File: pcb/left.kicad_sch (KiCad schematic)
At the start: 65 parts, among them SW1 SW_PUSH, SW10 SW_PUSH, SW11 SW_PUSH, SW12 SW_PUSH, SW13 SW_PUSH, SW14 SW_PUSH, SW15 SW_PUSH, SW16 SW_PUSH, SW17 SW_PUSH, SW18 SW_PUSH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

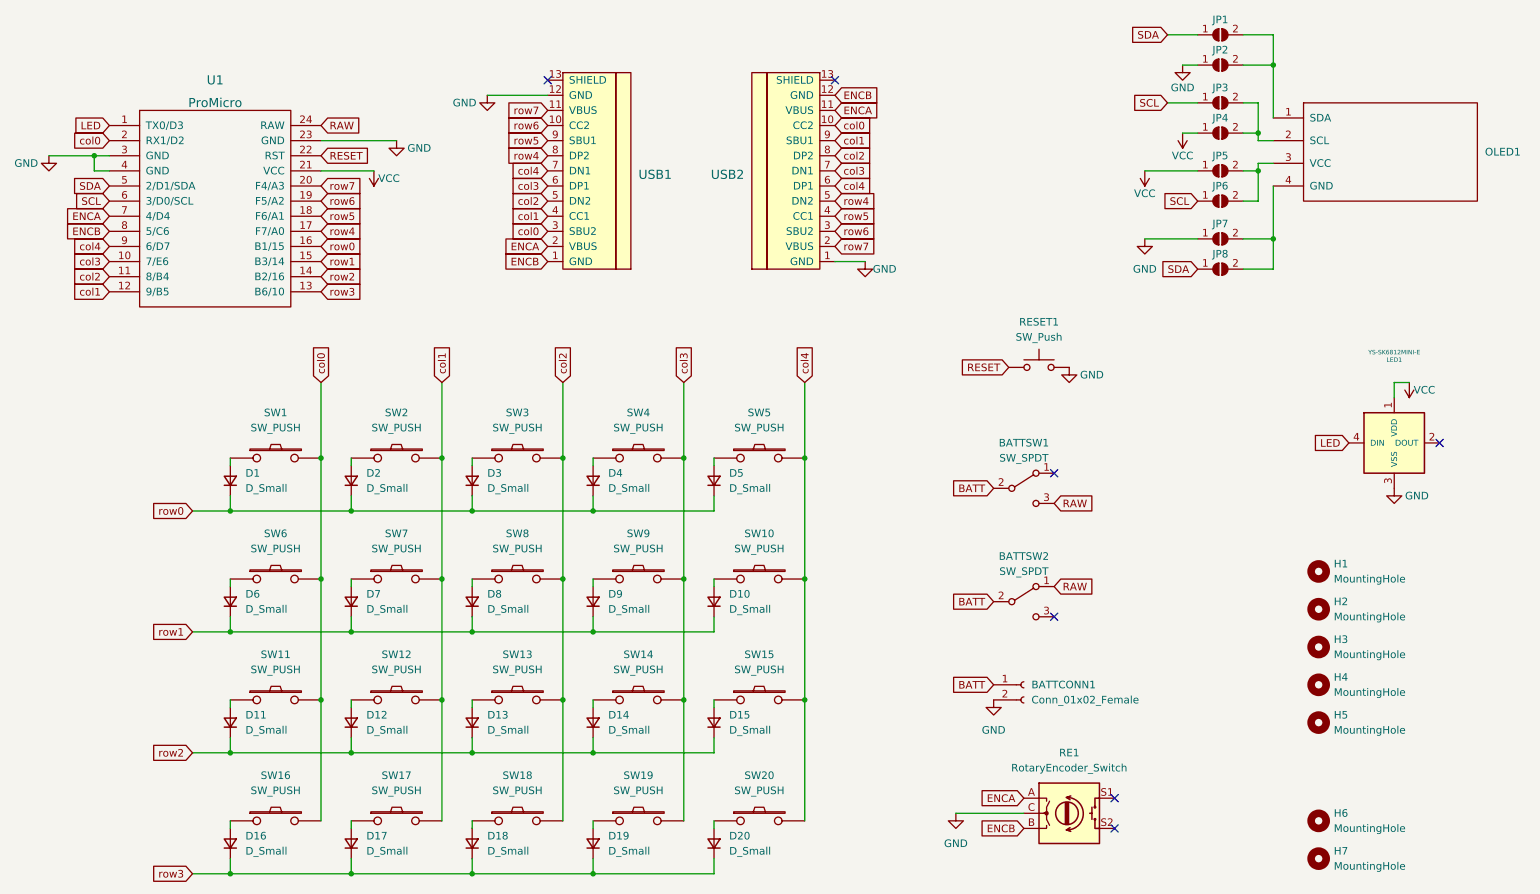
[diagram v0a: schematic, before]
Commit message: separate left and right sides
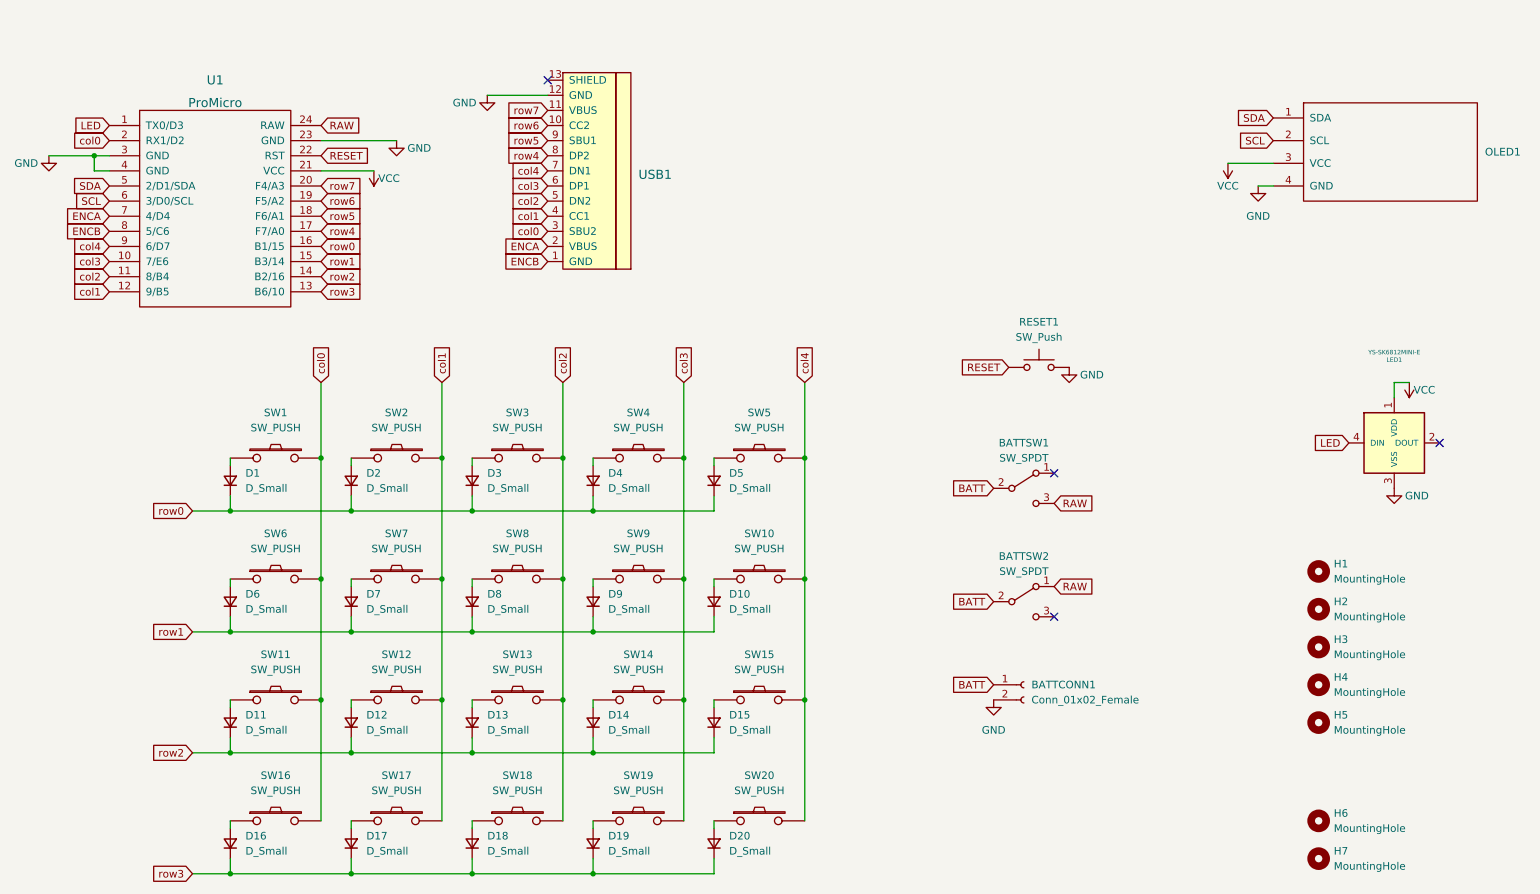
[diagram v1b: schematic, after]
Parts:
- removed JP1, JP2, JP3, JP4, JP5, JP6, JP7, JP8: SolderJumper_2_Open, Jumper:SolderJumper-2_P1.3mm_Open_TrianglePad1.0x1.5mm, symbol Jumper:SolderJumper_2_Open
- removed RE1: RotaryEncoder_Switch, pica:RotaryEncoder_EC11-no-legs, symbol Device:RotaryEncoder_Switch
- removed USB2: HRO-TYPE-C-31-M-12, typec:HRO-TYPE-C-31-M-12-HandSoldering, symbol typec:HRO-TYPE-C-31-M-12
- RESET1: footprint kbd:ResetSW -> kbd:ResetSW_1side
- U1: footprint keebio:ArduinoProMicro -> pica:ProMicro
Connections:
- net GND: now also OLED1.4 (GND)
- net SCL: now also OLED1.2 (SCL)
- net SDA: now also OLED1.1 (SDA)
- net VCC: now also OLED1.3 (VCC)
- no-connect marks 7 -> 4

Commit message: fix battery connector footprint
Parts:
- BATTCONN1: footprint Connector_JST:JST_XH_S2B-XH-A_1x02_P2.50mm_Horizontal -> Connector_JST:JST_PH_S2B-PH-K_1x02_P2.00mm_Horizontal
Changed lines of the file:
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@@
       (effects (font (size 1.27 1.27)) (justify left))
     )
-    (property "Footprint" "Connector_JST:JST_XH_S2B-XH-A_1x02_P2.50mm_Horizontal" (id 2) (at 187.96 129.54 0)
+    (property "Footprint" "Connector_JST:JST_PH_S2B-PH-K_1x02_P2.00mm_Horizontal" (id 2) (at 187.96 129.54 0)
       (effects (font (size 1.27 1.27)) hide)
     )
@@
     )
     (path "/39669874-ccc4-4e68-8529-233aa9d084b4"
-      (reference "BATTCONN1") (unit 1) (value "Conn_01x02_Female") (footprint "Connector_JST:JST_XH_S2B-XH-A_1x02_P2.50mm_Horizontal")
+      (reference "BATTCONN1") (unit 1) (value "Conn_01x02_Female") (footprint "Connector_JST:JST_PH_S2B-PH-K_1x02_P2.00mm_Horizontal")
     )
     (path "/b1f6a19b-fde1-4210-8161-211b835723ec"

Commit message: add full version
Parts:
- removed BATTSW2: SW_SPDT, Button_Switch_SMD:SW_SPDT_PCM12, symbol Switch:SW_SPDT
- removed LED1: YS-SK6812MINI-E, pica:SK6812-MINI-E, symbol kbd:YS-SK6812MINI-E
- removed OLED1: OLED, kbd:OLED_v2, symbol kbd:OLED
- removed RESET1: SW_Push, kbd:ResetSW_1side, symbol Switch:SW_Push
- removed U1: ProMicro, pica:ProMicro, symbol kbd:ProMicro
- added JP1, JP2: SolderJumper_2_Open, Jumper:SolderJumper-2_P1.3mm_Open_TrianglePad1.0x1.5mm, symbol Jumper:SolderJumper_2_Open
- added RE1: RotaryEncoder_Switch, pica:RotaryEncoder_EC11, symbol Device:RotaryEncoder_Switch
- added U1: xiao-ble, kleeb-mcu:xiao-ble-tht, symbol kleeb-mcu:xiao-ble
- USB1: footprint typec:HRO-TYPE-C-31-M-12-HandSoldering -> pica:HRO-TYPE-C-31-M-12-data
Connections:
- net row7 is gone; now on net VCC: USB1.11 (VBUS)
- net ENCA: now also RE1.A, U1.6 (A9_SCL/0.05_H); no longer USB1.2 (VBUS)
- net ENCB: now also USB1.5 (DN2), USB1.7 (DN1), JP1.1 (A), RE1.B; no longer USB1.1 (GND)
- net GND: now also USB1.1 (GND), RE1.C, U1.13 (GND), U1.18 (GND), U1.20 (GND)
- net RAW: now also U1.19 (BAT)
- net VCC: now also USB1.2 (VBUS), U1.12 (3V3)
- net col0: now also U1.1 (A2/0.02_H); no longer USB1.3 (SBU2)
- net col1: now also U1.2 (A4/0.03_H); no longer USB1.4 (CC1)
- net col2: now also U1.3 (A10/0.28); no longer USB1.5 (DN2)
- net col3: now also U1.4 (A11/0.29); no longer USB1.6 (DP1)
- net col4: now also U1.5 (A8_SDA/0.04_H); no longer USB1.7 (DN1)
- net row0: now also U1.11 (A6_MOSI/1.15)
- net row1: now also U1.10 (A5_MISO/1.14)
- net row2: now also U1.9 (A7_SCK/1.13)
- net row3: now also U1.8 (B9_RX/1.12)
- net row4 renamed DATA
- net DATA: now also USB1.6 (DP1), JP2.1 (A)
- net row5: no longer names the net of USB1.9 (SBU1)
- net row6: no longer names the net of USB1.10 (CC2)
- new net: JP1.2 (B), JP2.2 (B), U1.7 (B8_TX/1.11)
- no-connect marks 4 -> 14

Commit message: v2
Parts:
- added BATTCONN2: Conn_01x02_Female, pica:JST_PH_S2B-PH-K_1x02_P2.00mm, symbol Connector:Conn_01x02_Female
- added RE2: RotaryEncoder_Switch, pica:RotaryEncoder_EC11, symbol Device:RotaryEncoder_Switch
- BATTCONN1: footprint Connector_JST:JST_PH_S2B-PH-K_1x02_P2.00mm_Horizontal -> pica:JST_PH_S2B-PH-K_1x02_P2.00mm
- H1, H2, H3, H4, H5: footprint kbd:M2_HOLE_v2 -> pica:spacer_m2_3.4
- H6, H7: footprint kbd:M2_Hole_TH -> kbd:thread_m2
- SW1, SW10, SW11, SW12, SW13, SW14, SW15, SW16, SW17, SW18, SW19, SW2, SW3, SW4, SW5, SW6, SW7, SW8, SW9: footprint pica:CherryMX_Hotswap -> pica:CherryMX_Hotswap_ChocV2
- SW20: footprint pica:CherryMX_Hotswap_1.5 -> pica:CherryMX_Hotswap_ChocV2_1.5
- U1: footprint kleeb-mcu:xiao-ble-tht -> pica:xiao-ble-tht
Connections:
- net BATT: now also BATTCONN2.1 (Pin_1)
- net ENCA: now also RE2.A
- net ENCB: now also RE2.B
- net GND: now also BATTCONN2.2 (Pin_2), RE2.C
- no-connect marks 14 -> 16
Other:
- moved on the sheet: RE1

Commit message: remove second encoder
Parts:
- removed RE2: RotaryEncoder_Switch, pica:RotaryEncoder_EC11, symbol Device:RotaryEncoder_Switch
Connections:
- no-connect marks 16 -> 14
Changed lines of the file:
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@@
   (no_connect (at 106.68 29.21))
   (no_connect (at 163.83 55.88))
-  (no_connect (at 248.92 77.47))
   (no_connect (at 83.82 21.59))
-  (no_connect (at 248.92 82.55))
   (no_connect (at 248.92 57.15))
   (no_connect (at 163.83 30.48))
@@
     (stroke (width 0) (type default) (color 0 0 0 0))
   )
-  (wire (pts (xy 233.68 80.01) (xy 222.25 80.01))
-    (stroke (width 0) (type default) (color 0 0 0 0))
-  )
   (wire (pts (xy 135.89 118.11) (xy 135.89 120.65))
     (stroke (width 0) (type default) (color 0 0 0 0))
@@
     )
   )
-  (global_label "ENCB" (shape input) (at 233.68 82.55 180) (fields_autoplaced)
-    (effects (font (size 1.27 1.27)) (justify right))
-    (property "Intersheet References" "${INTERSHEET_REFS}" (id 0) (at 226.2474 82.4706 0)
-      (effects (font (size 1.27 1.27)) (justify right) hide)
-    )
-  )
   (global_label "col4" (shape input) (at 63.5 39.37 180) (fields_autoplaced)
     (effects (font (size 1.27 1.27)) (justify right))
@@
     (property "Intersheet References" "${INTERSHEET_REFS}" (id 0) (at 113.5683 44.5294 0)
       (effects (font (size 1.27 1.27)) (justify left) hide)
-    )
-  )
-  (global_label "ENCA" (shape input) (at 233.68 77.47 180) (fields_autoplaced)
-    (effects (font (size 1.27 1.27)) (justify right))
-    (property "Intersheet References" "${INTERSHEET_REFS}" (id 0) (at 226.4288 77.3906 0)
-      (effects (font (size 1.27 1.27)) (justify right) hide)
     )
   )
@@
     (pin "3")
   )
-  (symbol (lib_id "power:GND") (at 222.25 80.01 0) (unit 1)
-    (in_bom yes) (on_board yes)
-    (property "Reference" "#PWR0101" (id 0) (at 222.25 86.36 0)
-      (effects (font (size 1.27 1.27)) hide)
-    )
-    (property "Value" "GND" (id 1) (at 218.44 81.28 0))
-    (property "Footprint" "" (id 2) (at 222.25 80.01 0)
-      (effects (font (size 1.27 1.27)) hide)
-    )
-    (property "Datasheet" "" (id 3) (at 222.25 80.01 0)
-      (effects (font (size 1.27 1.27)) hide)
-    )
-    (pin "1")
-  )
   (symbol (lib_id "kbd:SW_PUSH") (at 143.51 111.76 0) (unit 1)
     (in_bom yes) (on_board yes) (fields_autoplaced)
@@
     )
   )
-  (symbol (lib_id "Device:RotaryEncoder_Switch") (at 241.3 80.01 0) (unit 1)
-    (in_bom yes) (on_board yes) (fields_autoplaced)
-    (property "Reference" "RE2" (id 0) (at 241.3 69.85 0))
-    (property "Value" "RotaryEncoder_Switch" (id 1) (at 241.3 72.39 0))
-    (property "Footprint" "pica:RotaryEncoder_EC11" (id 2) (at 237.49 75.946 0)
-      (effects (font (size 1.27 1.27)) hide)
-    )
-    (property "Datasheet" "~" (id 3) (at 241.3 73.406 0)
-      (effects (font (size 1.27 1.27)) hide)
-    )
-    (pin "A")
-    (pin "B")
-    (pin "C")
-    (pin "S1")
-    (pin "S2")
-  )
   (symbol (lib_id "kbd:SW_PUSH") (at 143.51 91.44 0) (unit 1)
     (in_bom yes) (on_board yes) (fields_autoplaced)
@@
       (reference "#PWR012") (unit 1) (value "GND") (footprint "")
     )
-    (path "/b78ffed6-3d23-423e-ac61-cdc8a8614879"
-      (reference "#PWR0101") (unit 1) (value "GND") (footprint "")
-    )
     (path "/ff6cca2a-3e50-4629-b2df-e89c9ae3661b"
       (reference "#PWR0102") (unit 1) (value "GND") (footprint "")
@@
       (reference "RE1") (unit 1) (value "RotaryEncoder_Switch") (footprint "pica:RotaryEncoder_EC11")
     )
-    (path "/fa123705-9e62-4b76-bfde-8f0ff234c8f1"
-      (reference "RE2") (unit 1) (value "RotaryEncoder_Switch") (footprint "pica:RotaryEncoder_EC11")
-    )
     (path "/dfe7bca9-eacf-484d-9fb9-819b1262f86e"

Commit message: udpate pcb, remove unused files
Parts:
- added J1: MJ-4PP-9, pica:MJ-4PP-9_1side, symbol kbd:MJ-4PP-9
- added JP3: SolderJumper_2_Open, Jumper:SolderJumper-2_P1.3mm_Open_TrianglePad1.0x1.5mm, symbol Jumper:SolderJumper_2_Open
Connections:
- net DATA: now also J1.A, JP3.1 (A); no longer JP2.1 (A)
- net ENCA: now also JP1.2 (B)
- net ENCB: now also JP2.1 (A), J1.B
- net GND: now also J1.C
- net VCC: now also J1.D
- net at JP2.2 (B), U1.7 (B8_TX/1.11): now also JP3.2 (B); no longer JP1.2 (B)
